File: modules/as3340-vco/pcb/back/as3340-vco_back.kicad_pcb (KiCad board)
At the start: 2 copper layers, 37.8 x 70.2 mm, 35 parts, among them J1 Conn_02x08_Odd_Even, J2 Conn_01x09, U1 AS3340, U2 L79L05_TO92

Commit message: modules: as3340-vco: fix references
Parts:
- J1: value Conn_02x08_Odd_Even -> IDC Header 2x8
- J2: value Conn_01x09 -> Pin Socket 1x9
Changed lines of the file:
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@@
   (page A4)
   (title_block
-    (title "as3340-vco back board")
+    (title "as3340-vco back")
     (date 2021-12-14)
     (rev 1.0)
@@
       (effects (font (size 1 1) (thickness 0.15)))
     )
-    (fp_text value Conn_01x09 (at 0 23.09) (layer F.Fab)
+    (fp_text value "Pin Socket 1x9" (at 0 23.09) (layer F.Fab)
       (effects (font (size 1 1) (thickness 0.15)))
     )
@@
       (effects (font (size 1 1) (thickness 0.15)) (justify mirror))
     )
-    (fp_text value Conn_02x08_Odd_Even (at 1.27 -23.88 270) (layer B.Fab)
-      (effects (font (size 1 1) (thickness 0.15)) (justify mirror))
-    )
+    (fp_text value "IDC Header 2x8" (at 1.27 -23.88 270) (layer B.Fab)
+      (effects (font (size 1 1) (thickness 0.15)) (justify mirror))
+    )

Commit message: modules: as3340-vco: back: upgrade to kicad 6
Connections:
- J1 pad 11: (no net) -> unconnected-(J1-Pad11)
- J1 pad 12: (no net) -> unconnected-(J1-Pad12)
- J1 pad 13: (no net) -> unconnected-(J1-Pad13)
- J1 pad 14: (no net) -> unconnected-(J1-Pad14)
- J1 pad 15: (no net) -> unconnected-(J1-Pad15)
- J1 pad 16: (no net) -> unconnected-(J1-Pad16)
- U1 pad 6: (no net) -> unconnected-(U1-Pad6)
- U1 pad 9: (no net) -> unconnected-(U1-Pad9)
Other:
- net class Default removed

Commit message: modules: as3340-vco: back: remove unconnected nets
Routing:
- net Net-(R9-Pad1): track 16.5 -> 15.9 mm
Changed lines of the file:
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@@
   (segment (start 161.163 90.932) (end 159.472 90.932) (width 0.4) (layer "F.Cu") (net 3))
   (segment (start 163.21449 92.98349) (end 161.163 90.932) (width 0.4) (layer "F.Cu") (net 3))
-  (segment (start 162.179 81.026) (end 161.798 81.026) (width 0.4) (layer "F.Cu") (net 3))
   (segment (start 163.21449 116.05851) (end 163.21449 92.98349) (width 0.4) (layer "F.Cu") (net 3))
   (segment (start 158.75 118.364) (end 160.909 118.364) (width 0.4) (layer "F.Cu") (net 3))
@@
   (segment (start 133.604 104.394) (end 135.255 104.394) (width 0.4) (layer "B.Cu") (net 14))
   (segment (start 140.97 83.566) (end 138.176 83.566) (width 0.4) (layer "B.Cu") (net 15))
-  (segment (start 132.842 94.488) (end 132.842 94.488) (width 0.4) (layer "F.Cu") (net 16))
+  (segment (start 132.334 81.026) (end 130.643 82.717) (width 0.4) (layer "F.Cu") (net 16))
+  (segment (start 145.669 114.427) (end 145.669 115.824) (width 0.4) (layer "F.Cu") (net 16))
   (segment (start 144.145 112.903) (end 145.669 114.427) (width 0.4) (layer "F.Cu") (net 16))
-  (segment (start 132.334 81.026) (end 130.643 82.717) (width 0.4) (layer "F.Cu") (net 16))
+  (segment (start 130.643 82.717) (end 130.643 83.439) (width 0.4) (layer "F.Cu") (net 16))
   (segment (start 133.223 112.903) (end 144.145 112.903) (width 0.4) (layer "F.Cu") (net 16))
-  (segment (start 130.643 82.717) (end 130.643 83.439) (width 0.4) (layer "F.Cu") (net 16))
-  (segment (start 145.669 114.427) (end 145.669 115.824) (width 0.4) (layer "F.Cu") (net 16))
   (segment (start 130.683 110.363) (end 133.223 112.903) (width 0.4) (layer "F.Cu") (net 16))
+  (segment (start 132.842 100.965) (end 130.683 103.124) (width 0.4) (layer "F.Cu") (net 16))
   (segment (start 132.842 94.488) (end 132.842 100.965) (width 0.4) (layer "F.Cu") (net 16))
-  (segment (start 132.842 100.965) (end 130.683 103.124) (width 0.4) (layer "F.Cu") (net 16))
+  (segment (start 130.683 103.124) (end 130.683 110.363) (width 0.4) (layer "F.Cu") (net 16))
   (segment (start 154.559 81.026) (end 132.334 81.026) (width 0.4) (layer "F.Cu") (net 16))
-  (segment (start 130.683 103.124) (end 130.683 110.363) (width 0.4) (layer "F.Cu") (net 16))
   (via (at 132.842 94.488) (size 0.8) (drill 0.4) (layers "F.Cu" "B.Cu") (net 16))
   (segment (start 156.163 129.239) (end 154.098 127.174) (width 0.4) (layer "B.Cu") (net 16))
-  (segment (start 132.842 85.638) (end 130.643 83.439) (width 0.4) (layer "B.Cu") (net 16))
   (segment (start 144.653 122.555) (end 147.701 125.603) (width 0.4) (layer "B.Cu") (net 16))
   (segment (start 156.718 86.106) (end 156.718 83.185) (width 0.4) (layer "B.Cu") (net 16))
@@
   (segment (start 156.718 83.185) (end 154.559 81.026) (width 0.4) (layer "B.Cu") (net 16))
   (segment (start 149.526 127.174) (end 147.701 128.999) (width 0.4) (layer "B.Cu") (net 16))
-  (segment (start 132.842 94.488) (end 132.842 85.638) (width 0.4) (layer "B.Cu") (net 16))
   (segment (start 147.701 128.999) (end 147.701 129.159) (width 0.4) (layer "B.Cu") (net 16))
   (segment (start 145.669 115.824) (end 145.669 117.983) (width 0.4) (layer "B.Cu") (net 16))
+  (segment (start 132.842 85.638) (end 130.643 83.439) (width 0.4) (layer "B.Cu") (net 16))
+  (segment (start 132.842 94.488) (end 132.842 85.638) (width 0.4) (layer "B.Cu") (net 16))
   (segment (start 154.098 127.174) (end 149.526 127.174) (width 0.4) (layer "B.Cu") (net 16))
   (segment (start 145.669 117.983) (end 144.653 118.999) (width 0.4) (layer "B.Cu") (net 16))
@@
   (segment (start 148.717 82.804) (end 148.717 85.598) (width 0.4) (layer "B.Cu") (net 22))
   (segment (start 148.717 85.598) (end 149.86 86.741) (width 0.4) (layer "B.Cu") (net 22))
-  (segment (start 150.241 86.36) (end 149.86 86.741) (width 0.4) (layer "B.Cu") (net 22))
   (segment (start 149.86 86.741) (end 147.32 89.281) (width 0.4) (layer "B.Cu") (net 22))
   (segment (start 153.924 82.804) (end 152.654 81.534) (width 0.4) (layer "B.Cu") (net 22))

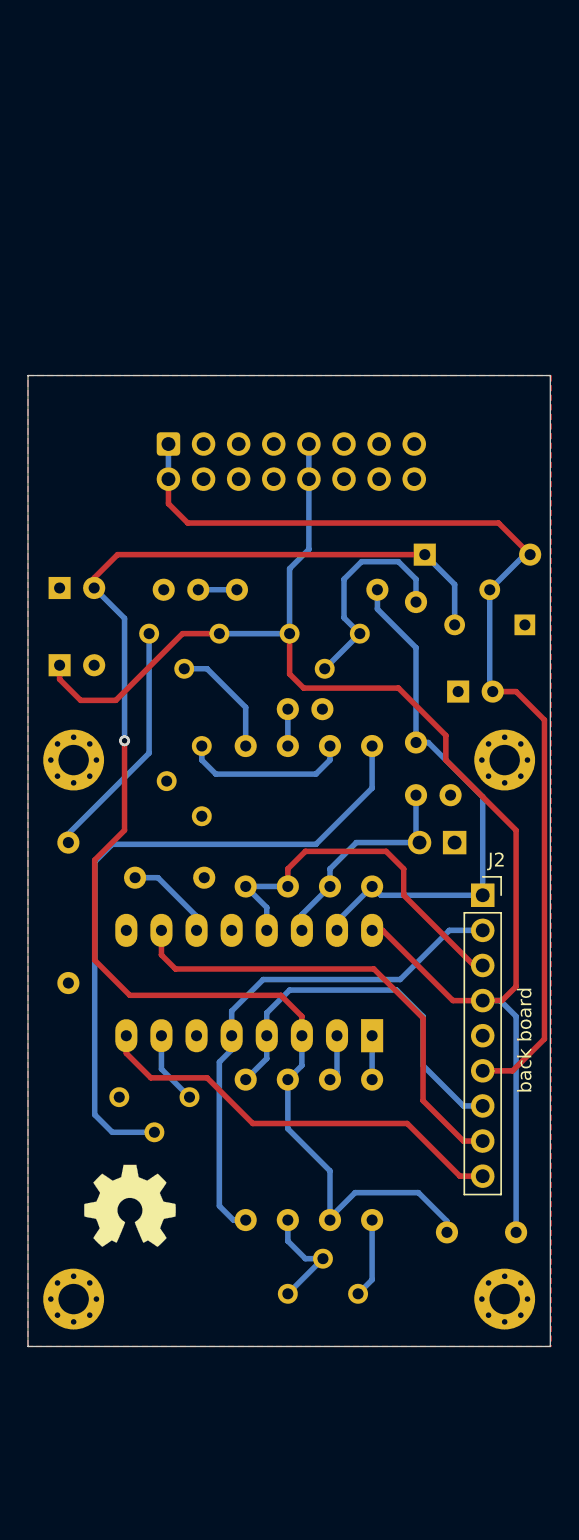
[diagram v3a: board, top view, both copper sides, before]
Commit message: modules: as3340-vco: back: revision A (redesign)
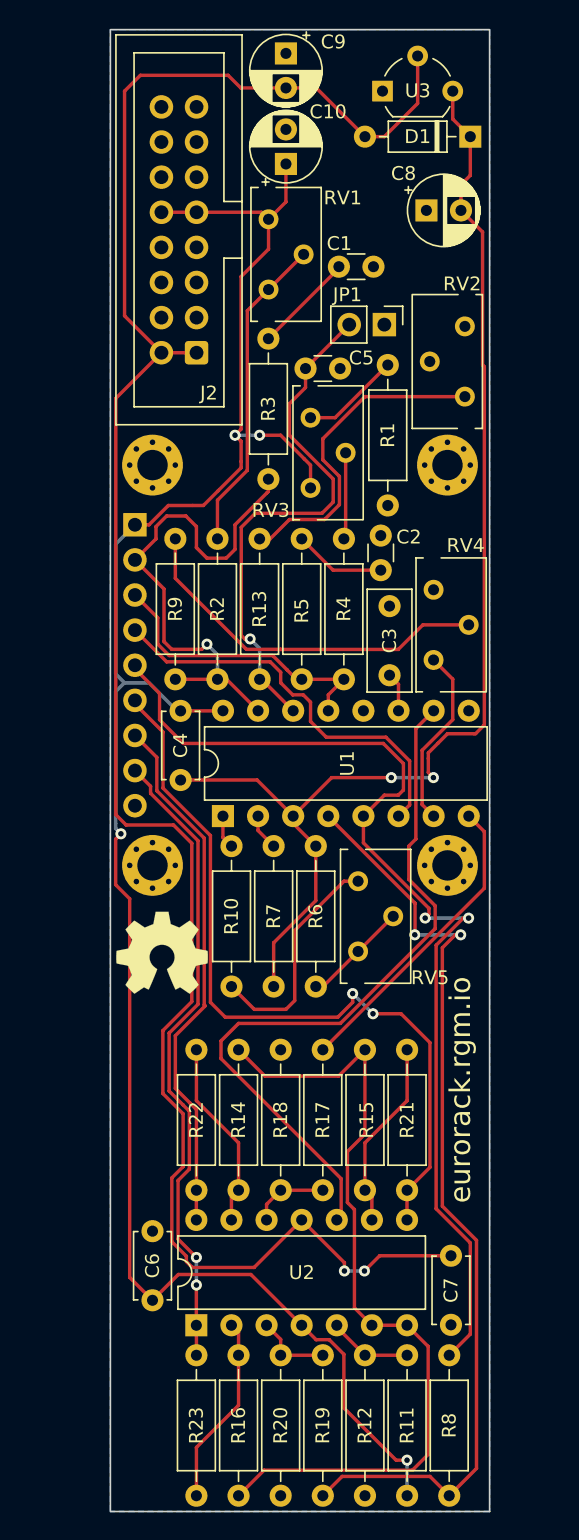
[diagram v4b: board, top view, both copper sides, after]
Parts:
- added C10: 10u, Capacitor_THT:CP_Radial_D5.0mm_P2.50mm, F.Cu at (144.5, 52.8)
- added C9: 10u, Capacitor_THT:CP_Radial_D5.0mm_P2.50mm, F.Cu at (144.5, 44.8)
- added R13: 1k62, Resistor_THT:R_Axial_DIN0207_L6.3mm_D2.5mm_P10.16mm_Horizontal, F.Cu at (142.6, 90.0)
- added R14: 100k, Resistor_THT:R_Axial_DIN0207_L6.3mm_D2.5mm_P10.16mm_Horizontal, F.Cu at (141.1, 127.0)
- added R15: 100k, Resistor_THT:R_Axial_DIN0207_L6.3mm_D2.5mm_P10.16mm_Horizontal, F.Cu at (150.2, 127.0)
- added R16: 100k, Resistor_THT:R_Axial_DIN0207_L6.3mm_D2.5mm_P10.16mm_Horizontal, F.Cu at (141.1, 138.9)
- added R17: 100k, Resistor_THT:R_Axial_DIN0207_L6.3mm_D2.5mm_P10.16mm_Horizontal, F.Cu at (147.2, 116.8)
- added R18: 100k, Resistor_THT:R_Axial_DIN0207_L6.3mm_D2.5mm_P10.16mm_Horizontal, F.Cu at (144.1, 127.0)
- added R19: 120k, Resistor_THT:R_Axial_DIN0207_L6.3mm_D2.5mm_P10.16mm_Horizontal, F.Cu at (147.2, 149.1)
- added R20: 68k, Resistor_THT:R_Axial_DIN0207_L6.3mm_D2.5mm_P10.16mm_Horizontal, F.Cu at (144.1, 138.9)
- added R21: 150k, Resistor_THT:R_Axial_DIN0207_L6.3mm_D2.5mm_P10.16mm_Horizontal, F.Cu at (153.3, 127.0)
- added R22: 150k, Resistor_THT:R_Axial_DIN0207_L6.3mm_D2.5mm_P10.16mm_Horizontal, F.Cu at (138.0, 127.0)
- added R23: 150k, Resistor_THT:R_Axial_DIN0207_L6.3mm_D2.5mm_P10.16mm_Horizontal, F.Cu at (138.0, 138.9)
- added R8: 10M, Resistor_THT:R_Axial_DIN0207_L6.3mm_D2.5mm_P10.16mm_Horizontal, F.Cu at (156.3, 149.1)
- added REF**: Eurorack_PCB_6HP, eurorack:Eurorack_PCB_6HP, F.Cu at (145.5, 96.6)
- added U3: L79L05_TO92, Package_TO_SOT_THT:TO-92_Wide, F.Cu at (151.5, 47.5)
- C1: value 560p -> 10n; footprint Capacitor_THT:C_Disc_D5.0mm_W2.5mm_P2.50mm -> Capacitor_THT:C_Disc_D3.0mm_W1.6mm_P2.50mm; moved to F.Cu
- C2: footprint Capacitor_THT:C_Disc_D5.0mm_W2.5mm_P2.50mm -> Capacitor_THT:C_Disc_D3.0mm_W1.6mm_P2.50mm; moved to F.Cu
- C3, C8, D1, JP1: moved to F.Cu
- C4: value 10n -> 100n; footprint Capacitor_THT:C_Disc_D5.0mm_W2.5mm_P2.50mm -> Capacitor_THT:C_Disc_D4.7mm_W2.5mm_P5.00mm; moved to F.Cu
- C5: value 10u -> 560p; footprint Capacitor_THT:CP_Radial_D5.0mm_P2.50mm -> Capacitor_THT:C_Disc_D3.0mm_W1.6mm_P2.50mm; moved to F.Cu
- C6: footprint Capacitor_THT:C_Disc_D4.3mm_W1.9mm_P5.00mm -> Capacitor_THT:C_Disc_D4.7mm_W2.5mm_P5.00mm; moved to F.Cu
- C7: value 10u -> 100n; footprint Capacitor_THT:CP_Radial_D5.0mm_P2.50mm -> Capacitor_THT:C_Disc_D4.7mm_W2.5mm_P5.00mm; moved to F.Cu
- H1, H2, H3, H4: value MountingHole -> MountingHole_Pad
- J1: value IDC Header 2x8 -> Pin Socket 1x9; footprint Connector_IDC:IDC-Header_2x08_P2.54mm_Vertical -> Connector_PinSocket_2.54mm:PinSocket_1x09_P2.54mm_Vertical
- J2: value Pin Socket 1x9 -> Eurorack PSU; footprint Connector_PinSocket_2.54mm:PinSocket_1x09_P2.54mm_Vertical -> eurorack:IDC-Header_2x08_P2.54mm_Vertical
- R1: value 18k -> 22k; moved to F.Cu
- R10: value 470R -> 18k; moved to F.Cu
- R11: value 10M -> 47k; moved to F.Cu
- R12: value 470k -> 18k; moved to F.Cu
- R2: value 5k6 -> 220k; moved to F.Cu
- R3: value 5k6 -> 470R; moved to F.Cu
- R4: value 22k -> 1M; moved to F.Cu
- R5: value 1k62 -> 470R; moved to F.Cu
- R6: value 1M -> 5k6; moved to F.Cu
- R7: value 470R -> 5k6; moved to F.Cu
- R9: value 220k -> 470k; moved to F.Cu
- RV1: value 5k -> 100k; moved to F.Cu
- RV2: value 10k -> 500R; moved to F.Cu
- RV3: value 500R -> 10k; moved to F.Cu
- RV4: value 100k -> 10k; moved to F.Cu
- RV5: value 10k -> 5k; moved to F.Cu
- U1: footprint Package_DIP:DIP-16_W7.62mm_LongPads -> Package_DIP:DIP-16_W7.62mm; moved to F.Cu
- U2: value L79L05_TO92 -> TL074; footprint Package_TO_SOT_THT:TO-92_Wide -> Package_DIP:DIP-14_W7.62mm; moved to F.Cu
- moved RV1 78.0 mm to (143.3, 56.8), turned to 0 degrees
- moved H2 66.1 mm to (156.2, 74.5), turned to 0 degrees
- moved U2 56.0 mm to (138.0, 136.8), turned to 90 degrees
- moved C7 55.5 mm to (156.5, 136.7), turned to 90 degrees
- moved R1 51.7 mm to (151.9, 67.3)
- moved R2 49.5 mm to (139.6, 79.9), turned to -90 degrees
- moved J2 44.4 mm to (138.0, 66.4), turned to 180 degrees
- moved R3 43.7 mm to (143.2, 75.6), turned to 90 degrees
- moved H3 40.4 mm to (134.9, 103.5), turned to 0 degrees
- moved C1 38.6 mm to (148.3, 60.2)
- moved JP1 37.8 mm to (151.6, 64.4), turned to -90 degrees
- moved C8 34.9 mm to (154.7, 56.1)
- moved R12 33.9 mm to (150.2, 138.9), turned to -90 degrees
- moved R11 32.3 mm to (153.3, 149.1), turned to 90 degrees
- moved D1 30.4 mm to (157.9, 50.8), turned to 180 degrees
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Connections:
- C1 pad 1: VS -> Net-(C1-Pad1)
- C4 pad 1: Net-(C4-Pad1) -> +12V
- C4 pad 2: GND -> -5V
- C5 pad 1: GND -> VS
- C5 pad 2: -5V -> GND
- C6 pad 2: -5V -> GND
- C7 pad 1: +12V -> GND
- C7 pad 2: GND -> -12V
- C8 pad 2: -12V -> -5V
- H1 pad 1: (no net) -> GND
- H2 pad 1: (no net) -> GND
- H3 pad 1: (no net) -> GND
- H4 pad 1: (no net) -> GND
- J1 pad 1: -12V -> +12V
- J1 pad 2: -12V -> VFCI
- J1 pad 3: GND -> VLFI
- J1 pad 4: GND -> VHSI
- J1 pad 5: GND -> VPWM
- J1 pad 6: GND -> OUT_TRIANGLE
- J1 pad 7: GND -> OUT_SAWTOOTH
- J1 pad 8: GND -> OUT_PULSE
- J1 pad 9: +12V -> GND
- J2 pad 1: VFCI -> -12V
- J2 pad 2: VPWM -> -12V
- J2 pad 3: VLFI -> GND
- J2 pad 4: +12V -> GND
- J2 pad 6: -12V -> GND
- J2 pad 7: VP -> GND
- J2 pad 8: VTO -> GND
- J2 pad 9: VSO -> +12V
- R1 pad 1: SCALE1 -> Net-(R1-Pad1)
- R1 pad 2: Net-(R1-Pad2) -> GND
- R10 pad 1: VFCI -> SCALE1
- R10 pad 2: Net-(C4-Pad1) -> Net-(R10-Pad2)
- R11 pad 1: VP -> +12V
- R11 pad 2: VPWM -> Net-(R11-Pad2)
- R12 pad 1: VFCI -> Net-(R11-Pad2)
- R12 pad 2: Net-(R12-Pad2) -> GND
- R2 pad 2: -5V -> VFCI
- R3 pad 1: SCALE2 -> VFCI
- R3 pad 2: -5V -> Net-(C1-Pad1)
- R4 pad 2: GND -> VLFI
- R5 pad 1: VS -> VLFI
- R5 pad 2: Net-(R5-Pad2) -> Net-(C2-Pad1)
- R6 pad 2: VLFI -> -5V
- R7 pad 1: VLFI -> SCALE2
- R7 pad 2: Net-(C2-Pad1) -> -5V
- R9 pad 1: Net-(R9-Pad1) -> VFCI
- R9 pad 2: VFCI -> Net-(R9-Pad2)
- RV1 pad 1: Net-(R1-Pad2) -> +12V
- RV2 pad 1: Net-(R4-Pad1) -> Net-(R13-Pad2)
- RV2 pad 2: Net-(R6-Pad1) -> GND
- RV2 pad 3: +12V -> GND
- RV3 pad 1: Net-(R5-Pad2) -> Net-(R1-Pad1)
- RV3 pad 2: GND -> Net-(R4-Pad1)
- RV3 pad 3: GND -> +12V
- RV4 pad 1: +12V -> GND
- RV4 pad 2: Net-(R9-Pad1) -> Net-(R9-Pad2)
- RV4 pad 3: Net-(R9-Pad1) -> VHFT
- RV5 pad 1: GND -> Net-(R10-Pad2)
- RV5 pad 2: Net-(R12-Pad2) -> Net-(R6-Pad1)
- RV5 pad 3: VHFT -> Net-(R6-Pad1)
- U1 pad 6: unconnected-(U1-Pad6) -> VHSI
- U2 pad 1: GND -> OUT_PULSE
- U2 pad 2: -12V -> Net-(R16-Pad1)
- U2 pad 3: -5V -> Net-(R19-Pad2)
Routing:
- net -12V: track 76.5 -> 147.2 mm, vias 0 -> 2
- net VREF: track 0.00 -> 59.4 mm
- net OUT_TRIANGLE: track 0.00 -> 56.5 mm, vias 0 -> 2
- net Net-(R12-Pad2): track 48.5 -> 0.00 mm
- net OUT_PULSE: track 0.00 -> 46.5 mm, vias 0 -> 2
- net +12V: track 102.4 -> 145.2 mm, vias 0 -> 4
- net VP: track 27.3 -> 68.0 mm, vias 0 -> 2
- net VPWM: track 37.4 -> 76.3 mm, vias 0 -> 2
- net OUT_SAWTOOTH: track 0.00 -> 38.7 mm
- net VHSI: track 0.00 -> 29.4 mm
- net Net-(R9-Pad2): track 0.00 -> 26.9 mm
- net Net-(R13-Pad2): track 0.00 -> 23.6 mm
- net VS: track 16.1 -> 38.5 mm, vias 0 -> 1
- net VTO: track 34.1 -> 52.8 mm
- net Net-(R10-Pad2): track 0.00 -> 16.6 mm
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- added copper zone on B.Cu, net GND
- removed copper zone on F.Cu, net GND
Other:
- board size 37.8 x 70.2 mm -> 27.4 x 107.2 mm
- board text added: "as3340-vco Rev. A"
- board text added: "back"
- board text removed: "AS3340-VCO r1.0"
- board text removed: "back board"
